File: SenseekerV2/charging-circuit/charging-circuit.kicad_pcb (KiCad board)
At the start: 2 copper layers, 40.8 x 83.5 mm, 91 parts, among them J1 2.54-1*6PHeader-RA, Q1 2N7002, Q2 CJQ4435, Q3 currentmirror, Q4 2N7002, Q5 CJQ4435, Q6 2N7002, Q7 CJQ4435, U1 MAX17048G+T10, U10 BQ25606RGER, U11 Battery Input, U2 MT3608, U3 MT3608, U6 MT3608, U7 2.54-2*20, U8 MAX3232CDBR, U9 ADS1115IDGSR

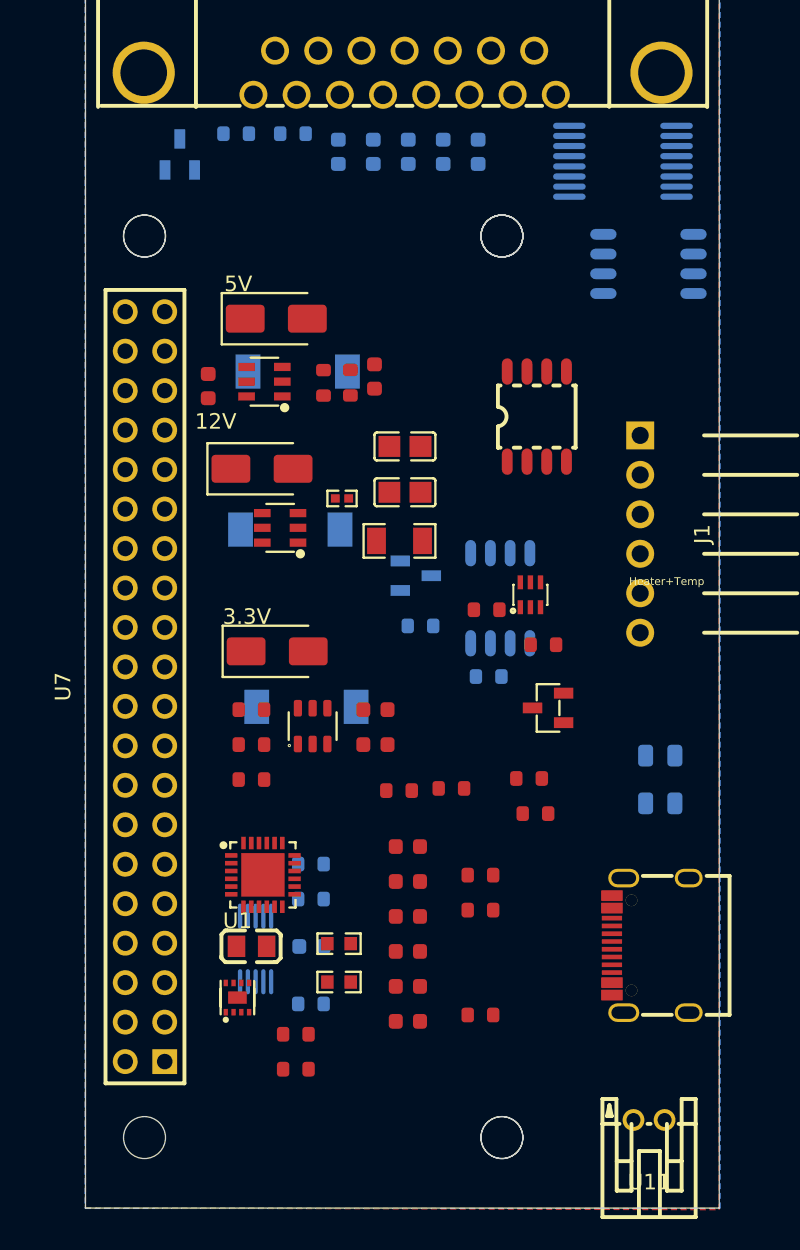
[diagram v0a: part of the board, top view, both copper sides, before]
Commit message: Initial Traces Complete
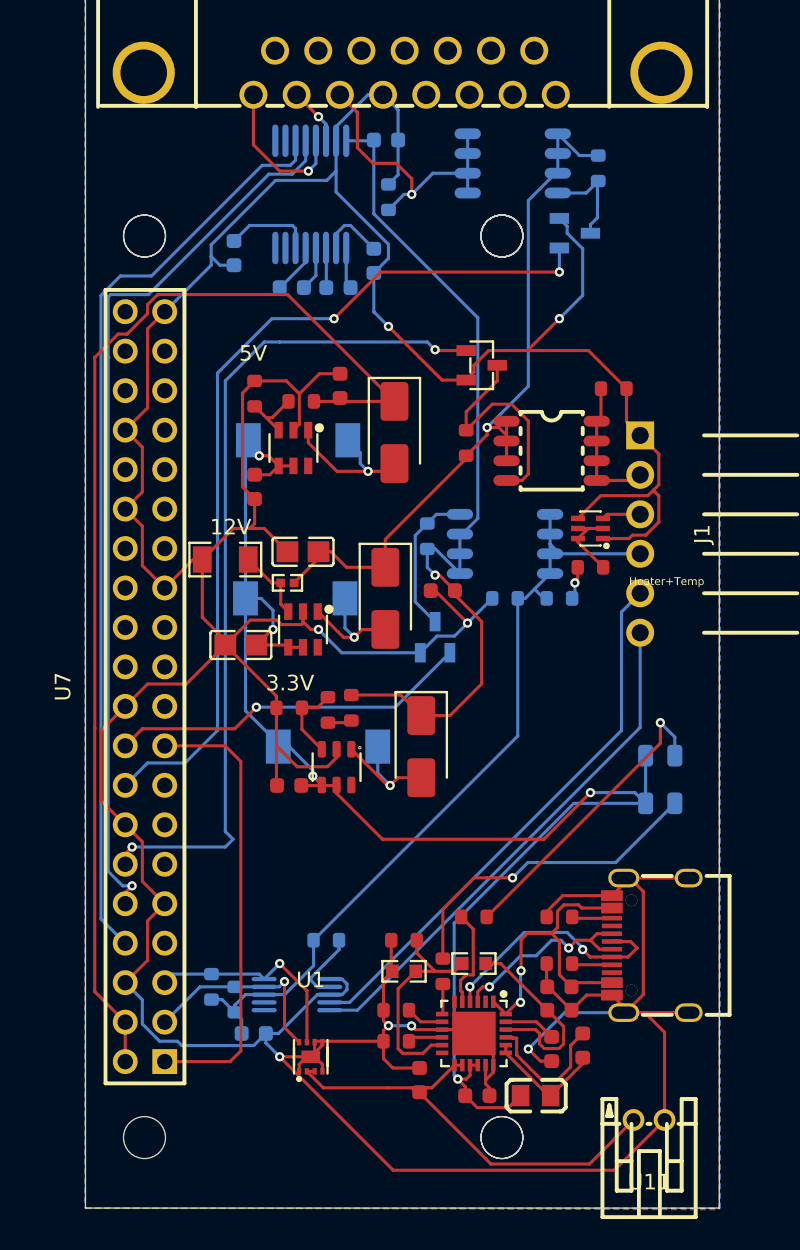
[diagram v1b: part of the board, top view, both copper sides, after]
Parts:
- R4: moved to B.Cu
- moved Q6 25.9 mm to (131.5, 90.5), turned to 180 degrees
- moved RPROG5 25.7 mm to (134.0, 100.5)
- moved R14 24.3 mm to (124.5, 104.0), turned to -90 degrees
- moved R15 23.4 mm to (133.0, 86.3), turned to 90 degrees
- moved Q1 22.5 mm to (125.5, 99.0), turned to 180 degrees
- moved L4 20.7 mm to (129.0, 146.0), turned to 180 degrees
- moved U8 20.2 mm to (114.5, 88.0), turned to 180 degrees
- moved R30 18.6 mm to (130.5, 134.5), turned to 180 degrees
- moved R31 18.3 mm to (130.5, 137.5), turned to 180 degrees
- moved U10 17.0 mm to (125.0, 142.0), turned to -90 degrees
- moved R22 16.7 mm to (120.0, 142.5)
- moved C2 16.6 mm to (110.0, 117.0), turned to 0 degrees
- moved C13 14.2 mm to (130.0, 143.0), turned to 90 degrees
- moved R25 14.1 mm to (120.0, 140.5)
- moved C9 13.3 mm to (130.5, 139.0)
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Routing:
- net GND: track 0.00 -> 353.5 mm, vias 0 -> 8
- net /VSYS: track 0.00 -> 99.9 mm, vias 0 -> 5
- net /5 Vout: track 0.00 -> 75.6 mm
- net /GPIO14/TXD0: track 0.00 -> 59.7 mm
- net /GPIO15/RXD0: track 0.00 -> 57.9 mm, vias 0 -> 1
- net /GPIO23: track 0.00 -> 56.6 mm, vias 0 -> 2
- net /3.3V: track 0.00 -> 55.9 mm, vias 0 -> 1
- net /GPIO18/PCM.CLK: track 0.00 -> 54.5 mm, vias 0 -> 2
- net /Temp3.3V: track 0.00 -> 52.7 mm
- net /12V: track 0.00 -> 47.1 mm, vias 0 -> 1
- net /A0: track 0.00 -> 35.4 mm
- net /A1: track 0.00 -> 33.6 mm
- net /raspi3.3V: track 0.00 -> 29.1 mm
- net /VBAT: track 0.00 -> 29.0 mm
- net /GPIO24: track 0.00 -> 23.4 mm, vias 0 -> 1
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
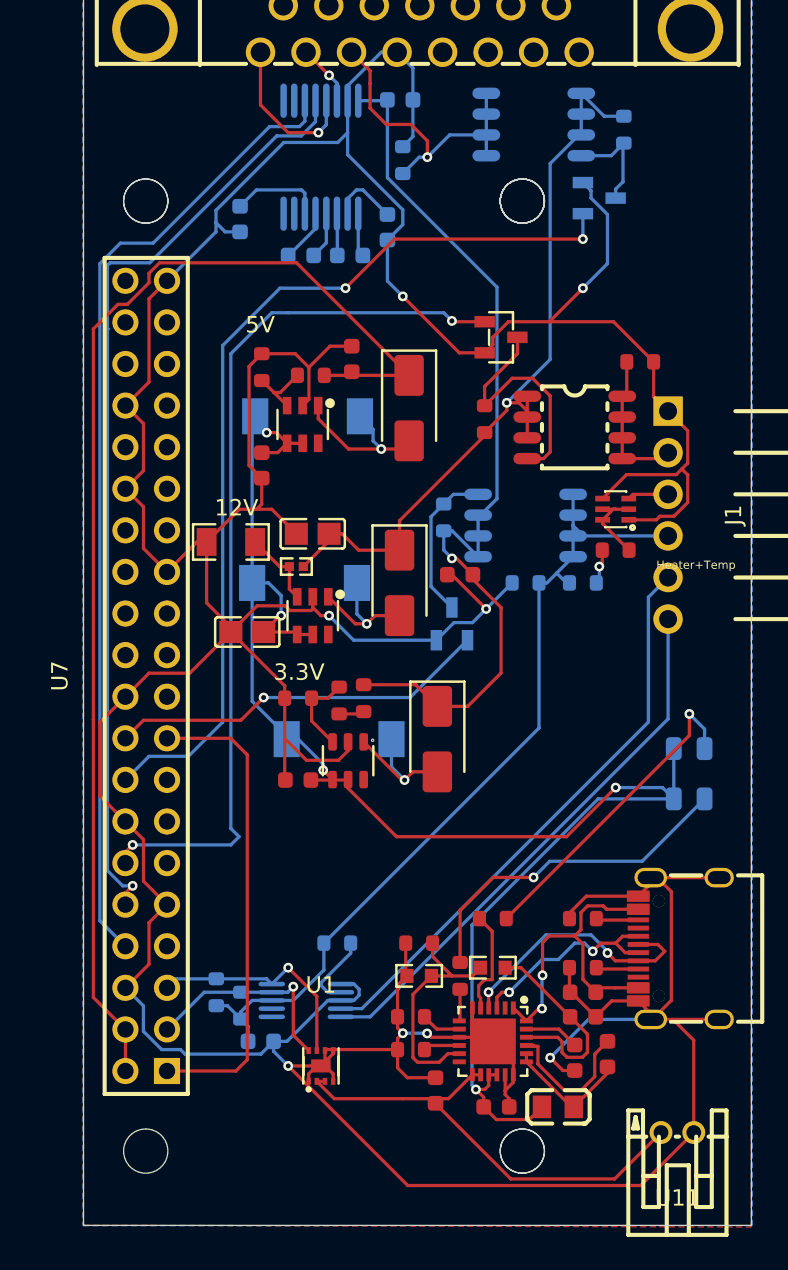
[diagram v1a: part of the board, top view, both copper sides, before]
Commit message: Fixed DRC Thermal Errors
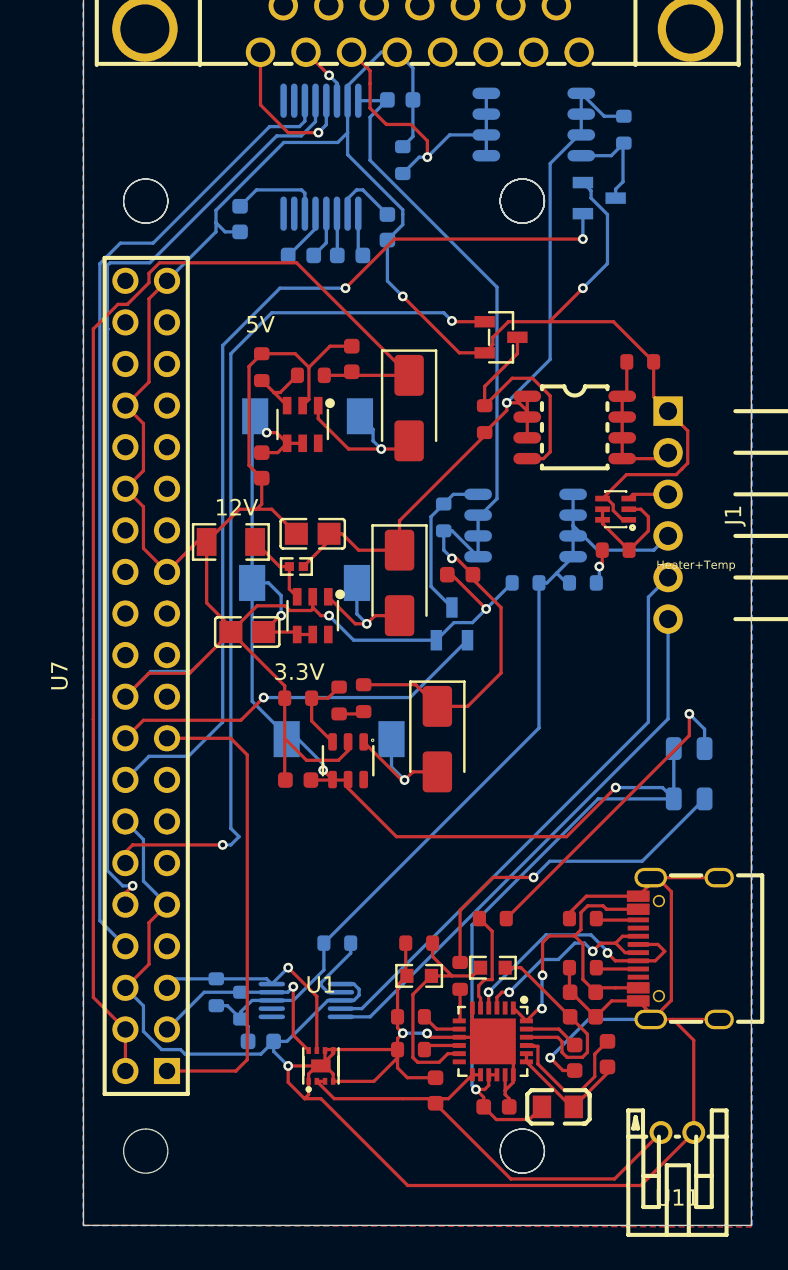
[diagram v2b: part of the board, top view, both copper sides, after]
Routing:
- net /base: track 5.19 -> 7.09 mm
- net GND: track 353.5 -> 352.2 mm
- net /3.3V: track 55.9 -> 56.7 mm
- net /Temp3.3V: track 52.7 -> 53.4 mm

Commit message: Final Edits to v2 before sending to Lucas
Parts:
- removed the ? at (40.1, 122.1)
- removed the ? at (63.1, 64.0) (x4)
- removed the ? at (40.1, 64.0) (x2)
- removed the ? at (63.1, 122.1) (x2)
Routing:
- net /VSYS: track 99.9 -> 100.6 mm
- net Net-(D8-Pad1): track 19.6 -> 20.3 mm

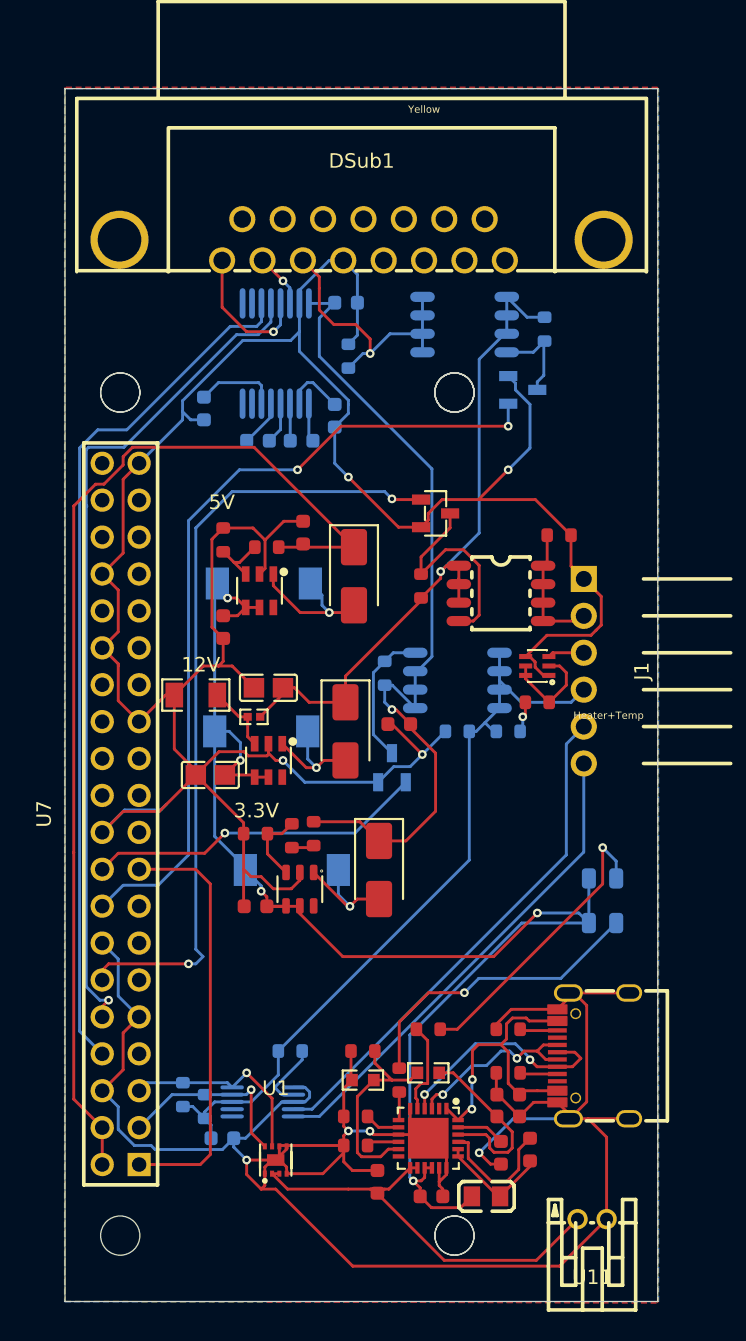
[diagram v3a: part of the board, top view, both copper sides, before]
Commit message: Brning in pcb from front of DSUB
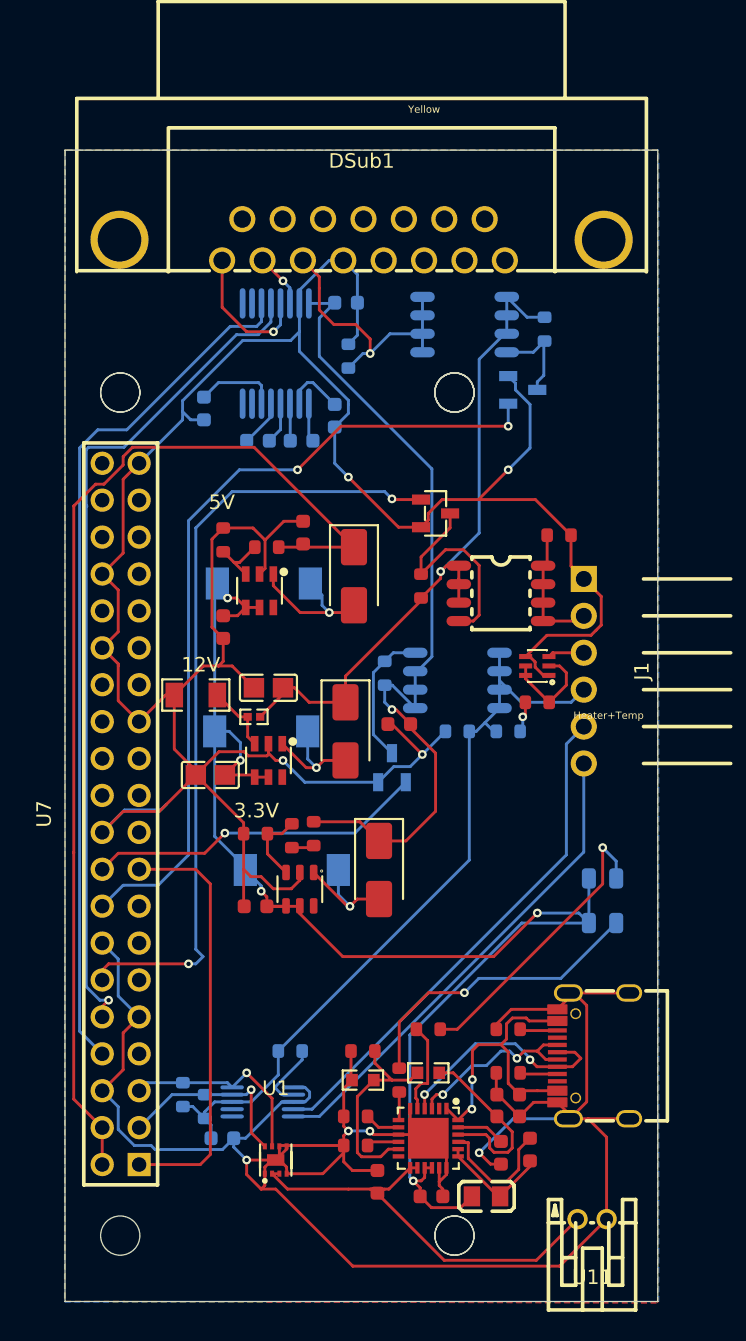
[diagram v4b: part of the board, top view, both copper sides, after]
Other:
- board size 40.8 x 83.5 mm -> 40.8 x 79.2 mm
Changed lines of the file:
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@@
 	)
 	(gr_rect
-		(start 100 69.76625)
+		(start 100 74)
 		(end 140.79 153.23625)
 		(stroke
@@
 		(polygon
 			(pts
-				(xy 100 69.668613) (xy 100 153.225476) (xy 140.78 153.342167) (xy 140.78 69.673819)
+				(xy 100 74) (xy 100 153.225476) (xy 140.78 153.342167) (xy 140.78 74)
 			)
 		)
@@
 		(polygon
 			(pts
-				(xy 99.97 69.768686) (xy 99.97 153.258686) (xy 140.85 153.258686) (xy 140.85 69.768686)
+				(xy 100 74) (xy 99.97 153.258686) (xy 140.85 153.258686) (xy 140.85 74)
 			)
 		)

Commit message: fixed dsub
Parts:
- removed DSub1: DS1037-15FNAKT74-0CC, easyeda2kicad:DSUB-TH_DS1037-15FNAKT74-0CC
- added DSub2: DS1038-15FBNSIA74-0CC, easyeda2kicad:DSUB-TH_DS1038-15FBNSIA74-0CC, F.Cu at (119.4, 77.7)
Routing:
- net /UART_RX_13V: track 9.61 -> 12.2 mm
- net Net-(DSub2-Pad3): track 19.1 -> 21.0 mm
- net /UART_TX_13V: track 3.74 -> 5.65 mm
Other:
- board size 40.8 x 79.2 mm -> 40.8 x 83.5 mm

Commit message: breakout
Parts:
- removed ? (x9): , 
- removed DSub2: DS1038-15FBNSIA74-0CC, easyeda2kicad:DSUB-TH_DS1038-15FBNSIA74-0CC
- removed Q4, Q6: 2N7002, easyeda2kicad:SOT-23-3_L2.9-W1.3-P1.90-LS2.4-BR
- removed Q5, Q7: CJQ4435, easyeda2kicad:SOP-8_L5.0-W4.0-P1.27-LS6.2-BL
- removed R15, R16: 10kΩ, PCM_JLCPCB:R_0603
- removed RPROG4, RPROG6: 1kΩ, PCM_JLCPCB:R_0603
- added C3: 100nF, PCM_JLCPCB:C_0603, F.Cu at (208.6, 127.5)
- added H1: Header-Male-2.54_1x6, easyeda2kicad:HDR-TH_6P-P2.54-V-M-1, F.Cu at (79.3, 73.7)
- added H2: 77311-462K05LF, easyeda2kicad:HDR-TH_5P-P2.54-V-M, F.Cu at (159.4, 126.0)
- added H3: Header-Male-2.54_1x6, easyeda2kicad:HDR-TH_6P-P2.54-V-M-1, F.Cu at (114.6, 35.2)
- added H4: Header-Male-2.54_1x6, easyeda2kicad:HDR-TH_6P-P2.54-V-M-1, F.Cu at (245.6, 76.1)
- added P1: Header-Male-2.54_2x2, easyeda2kicad:HDR-TH_4P-P2.54-V-M-R2-C2-S2.54-1, F.Cu at (67.2, 73.6)
- added P2: Header-Male-2.54_2x2, easyeda2kicad:HDR-TH_4P-P2.54-V-M-R2-C2-S2.54-1, F.Cu at (250.3, 112.0)
- added P3: 1.27mm/1*3p, easyeda2kicad:HDR-TH_3P-P1.27-V-M-1, F.Cu at (213.8, 118.0)
- added P5: 1.27mm/1*3p, easyeda2kicad:HDR-TH_3P-P1.27-V-M-1, F.Cu at (100.2, 41.3)
- added P6: 1.27mm/1*3p, easyeda2kicad:HDR-TH_3P-P1.27-V-M-1, F.Cu at (77.1, 41.3)
- added P7: 1.27mm/1*3p, easyeda2kicad:HDR-TH_3P-P1.27-V-M-1, F.Cu at (58.8, 36.5)
- added Q8: CJQ4435, easyeda2kicad:SOP-8_L5.0-W4.0-P1.27-LS6.2-BL, F.Cu at (219.5, 124.2)
- added R5: 44.2kohm, easyeda2kicad:R0402, F.Cu at (203.6, 125.8)
- added R6: 62kohm, easyeda2kicad:R0805, F.Cu at (204.4, 123.3)
- added R7: 30kΩ, PCM_JLCPCB:R_0603, F.Cu at (214.1, 121.1)
- added R8: 10kΩ, PCM_JLCPCB:R_0603, F.Cu at (214.1, 123.4)
- added R9: 10kΩ, PCM_JLCPCB:R_0603, F.Cu at (214.1, 125.6)
- added REF**: BreakLine_5h_D0.5mm_P0.85mm, MouseBites:BreakLine_5h_D0.5mm_P0.85mm, F.Cu at (64.0, 53.8)
- added REF**: BreakLine_5h_D0.5mm_P0.85mm, MouseBites:BreakLine_5h_D0.5mm_P0.85mm, F.Cu at (106.5, 53.8)
- added REF**: BreakLine_5h_D0.5mm_P0.85mm, MouseBites:BreakLine_5h_D0.5mm_P0.85mm, F.Cu at (104.3, 51.2)
- added REF**: BreakLine_5h_D0.5mm_P0.85mm, MouseBites:BreakLine_5h_D0.5mm_P0.85mm, F.Cu at (59.7, 53.8)
- added REF**: BreakLine_5h_D0.5mm_P0.85mm, MouseBites:BreakLine_5h_D0.5mm_P0.85mm, F.Cu at (55.5, 53.8)
- added REF**: BreakLine_5h_D0.5mm_P0.85mm, MouseBites:BreakLine_5h_D0.5mm_P0.85mm, F.Cu at (104.3, 33.9)
- added REF**: BreakLine_5h_D0.5mm_P0.85mm, MouseBites:BreakLine_5h_D0.5mm_P0.85mm, F.Cu at (97.8, 53.8)
- added REF**: BreakLine_5h_D0.5mm_P0.85mm, MouseBites:BreakLine_5h_D0.5mm_P0.85mm, F.Cu at (47.1, 53.8)
- added REF**: BreakLine_5h_D0.5mm_P0.85mm, MouseBites:BreakLine_5h_D0.5mm_P0.85mm, F.Cu at (104.3, 46.8)
- added REF**: BreakLine_5h_D0.5mm_P0.85mm, MouseBites:BreakLine_5h_D0.5mm_P0.85mm, F.Cu at (104.2, 42.3)
- added REF**: BreakLine_5h_D0.5mm_P0.85mm, MouseBites:BreakLine_5h_D0.5mm_P0.85mm, F.Cu at (93.5, 53.8)
- added REF**: BreakLine_5h_D0.5mm_P0.85mm, MouseBites:BreakLine_5h_D0.5mm_P0.85mm, F.Cu at (81.0, 53.8)
- added REF**: BreakLine_5h_D0.5mm_P0.85mm, MouseBites:BreakLine_5h_D0.5mm_P0.85mm, F.Cu at (110.8, 53.8)
- added REF**: BreakLine_5h_D0.5mm_P0.85mm, MouseBites:BreakLine_5h_D0.5mm_P0.85mm, F.Cu at (72.4, 53.8)
- added REF**: BreakLine_5h_D0.5mm_P0.85mm, MouseBites:BreakLine_5h_D0.5mm_P0.85mm, F.Cu at (115.0, 53.8)
- added REF**: BreakLine_5h_D0.5mm_P0.85mm, MouseBites:BreakLine_5h_D0.5mm_P0.85mm, F.Cu at (68.1, 53.8)
- added REF**: BreakLine_5h_D0.5mm_P0.85mm, MouseBites:BreakLine_5h_D0.5mm_P0.85mm, F.Cu at (85.1, 53.8)
- added REF**: BreakLine_5h_D0.5mm_P0.85mm, MouseBites:BreakLine_5h_D0.5mm_P0.85mm, F.Cu at (104.2, 37.9)
- added REF**: BreakLine_5h_D0.5mm_P0.85mm, MouseBites:BreakLine_5h_D0.5mm_P0.85mm, F.Cu at (123.4, 53.8)
- added REF**: BreakLine_5h_D0.5mm_P0.85mm, MouseBites:BreakLine_5h_D0.5mm_P0.85mm, F.Cu at (102.0, 53.8)
- added REF**: BreakLine_5h_D0.5mm_P0.85mm, MouseBites:BreakLine_5h_D0.5mm_P0.85mm, F.Cu at (119.3, 53.8)
- added REF**: BreakLine_5h_D0.5mm_P0.85mm, MouseBites:BreakLine_5h_D0.5mm_P0.85mm, F.Cu at (89.4, 53.8)
- added REF**: BreakLine_5h_D0.5mm_P0.85mm, MouseBites:BreakLine_5h_D0.5mm_P0.85mm, F.Cu at (51.3, 53.8)
- added REF**: BreakLine_5h_D0.5mm_P0.85mm, MouseBites:BreakLine_5h_D0.5mm_P0.85mm, F.Cu at (76.5, 53.8)
- added RPROG1: 1kΩ, PCM_JLCPCB:R_0603, F.Cu at (214.1, 127.9)
- added U4: TPL5110DDCT, easyeda2kicad:TSOT-23-6_L2.9-W1.6-P0.95-LS2.8-BR, F.Cu at (208.8, 123.9)
- added U5: BQ25606RGER, easyeda2kicad:VQFN-24_L4.0-W4.0-P0.50-TL-EP2.8, F.Cu at (104.9, 61.3)
- added mouse-bite-2mm-slot: VAL**, MouseBites:mouse-bite-2mm-slot, F.Cu at (26.7, 66.2)
- added mouse-bite-2mm-slot: VAL**, MouseBites:mouse-bite-2mm-slot, F.Cu at (28.4, 60.9)
- C12, C17, C18, C19, C20, C21, D8, D9, L1, L2, L3, R12, R13, R21, R4, U8, U9: moved to F.Cu
- U7: value 2.54-2*20 -> Z-21320110021001; footprint easyeda2kicad:HDR-TH_40P-P2.54-V-F-R2-C20-S2.54 -> easyeda2kicad:HDR-TH_20P-P2.54-V-M-R2-C10-S2.54
- moved R12 156.5 mm to (237.4, 50.8), turned to 0 degrees
- moved U9 154.1 mm to (242.4, 54.9), turned to 0 degrees
- moved C12 152.9 mm to (237.4, 56.1)
- moved R21 150.8 mm to (237.4, 59.8), turned to 0 degrees
- moved R13 147.4 mm to (237.4, 53.1)
- moved U1 134.1 mm to (245.1, 112.8)
- moved Q2 129.2 mm to (247.5, 50.7), turned to 0 degrees
- moved J1 129.2 mm to (254.1, 58.3)
- moved R14 127.0 mm to (248.8, 77.7), turned to 0 degrees
- moved Q1 126.2 mm to (248.2, 69.5), turned to 0 degrees
- moved R4 125.3 mm to (245.7, 64.6)
- moved R23 125.2 mm to (249.3, 66.8)
- moved Q3 124.0 mm to (247.1, 62.2), turned to 0 degrees
- moved RPROG5 117.1 mm to (248.4, 75.4)
- moved D6 113.1 mm to (49.8, 36.1), turned to 0 degrees
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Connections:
- C1 pad 1: GND -> /12GND
- C1 pad 2: /12V -> /12VOUT
- C10 pad 1: /VSYS -> /3V3VSYS
- C10 pad 2: GND -> /3V3GND
- C11 pad 1: GND -> /3V3GND
- C11 pad 2: /3.3V -> /3V3VOUT
- C12 pad 2: GND -> /Address
- C13 pad 1: GND -> /GND1
- C14 pad 1: GND -> /GND1
- C14 pad 2: /VBAT -> /VBAT1
- C15 pad 2: GND -> /GND1
- C17 pad 2: GND -> /DSUBGND
- C18 pad 2: GND -> /DSUBGND
- C2 pad 1: GND -> /12GND
- C2 pad 2: /VSYS -> /12VSYS
- C21 pad 2: GND -> /DSUBGND
- C22 pad 1: GND -> /GND1
- C22 pad 2: /VSYS -> /VSYS1
- C4 pad 1: GND -> /5GND
- C4 pad 2: /5 Vout -> /5VOUT
- C7 pad 1: /VSYS -> /5VSYS
- C7 pad 2: GND -> /5GND
- C9 pad 1: GND -> /GND1
- C9 pad 2: /VBUS -> /VBUS1
- D4 pad 1: /12V -> /12VOUT
- D5 pad 1: /5 Vout -> /5VOUT
- D6 pad 1: /3.3V -> /3V3VOUT
- D8 pad 2: /VSYS -> /VSYS1
- D9 pad 2: /VSYS -> /VSYS1
- J1 pad 1: GND -> /Address
- L1 pad 1: /VSYS -> /5VSYS
- L2 pad 1: /VSYS -> /12VSYS
- L3 pad 1: /VSYS -> /3V3VSYS
- L4 pad 2: /VSYS -> /VSYS1
- Q1 pad 1: /GPIO18/PCM.CLK -> /PWMSIG
- Q1 pad 2: GND -> /Address
- Q2 pad 1: /12V -> /TEMP12V
- Q2 pad 2: /12V -> /TEMP12V
- Q2 pad 3: /12V -> /TEMP12V
- Q3 pad 1: GND -> /Address
- Q3 pad 4: GND -> /Address
- R1 pad 1: GND -> /12GND
- R10 pad 1: /5 Vout -> /5VOUT
- R12 pad 2: /GPIO3/SCL1 -> /TEMPSCL
- R14 pad 2: /12V -> /TEMP12V
- R18 pad 1: /3.3V -> /3V3VOUT
- R19 pad 2: GND -> /3V3GND
- R2 pad 1: /12V -> /12VOUT
- R21 pad 2: /GPIO2/SDA1 -> /TEMPSDA
- R22 pad 1: GND -> /GND1
- R25 pad 1: GND -> /GND1
- R27 pad 1: /REGN -> /REGN1
- R28 pad 2: GND -> /GND1
- R29 pad 2: GND -> /GND1
- R3 pad 2: GND -> /5GND
- R30 pad 2: GND -> /USBGND
- R31 pad 2: GND -> /USBGND
- RPROG5 pad 2: GND -> /Address
- U1 pad 1: GND -> /FUELGND
- U1 pad 2: /VBAT -> /FUELBAT
- U1 pad 3: /VBAT -> /FUELBAT
- U1 pad 4: GND -> /FUELGND
- U1 pad 5: GND -> /FUELGND
- U1 pad 6: GND -> /FUELGND
- U1 pad 7: /GPIO3/SCL1 -> /FUELSCL
- U1 pad 8: /GPIO2/SDA1 -> /FUELSDA
- U1 pad 9: GND -> /FUELGND
- U10 pad 1: /VBUS -> /VBUS1
- U10 pad 13: /VBAT -> /VBAT1
- U10 pad 14: /VBAT -> /VBAT1
- U10 pad 15: /VSYS -> /VSYS1
- U10 pad 16: /VSYS -> /VSYS1
- U10 pad 17: GND -> /GND1
- U10 pad 18: GND -> /GND1
- U10 pad 24: /VBUS -> /VBUS1
- U10 pad 25: GND -> /GND1
- U10 pad 3: /D+ -> /1D+
- U10 pad 4: /D- -> /1D-
- U10 pad 6: GND -> unconnected-(U10-OTG-Pad6)
- U10 pad 9: GND -> /GND1
- U11 pad 2: GND -> /USBGND
- U2 pad 2: GND -> /5GND
- U2 pad 4: /VSYS -> /5VSYS
- U2 pad 5: /VSYS -> /5VSYS
- U3 pad 2: GND -> /12GND
- U3 pad 4: /VSYS -> /12VSYS
- U3 pad 5: /VSYS -> /12VSYS
- U6 pad 2: GND -> /3V3GND
- U6 pad 4: /VSYS -> /3V3VSYS
- U6 pad 5: /VSYS -> /3V3VSYS
- U7 pad 1: /raspi3.3V -> /VAC2
- U7 pad 10: /GPIO15/RXD0 -> /ICHG2
- U7 pad 11: /GPIO17 -> /TS2
- U7 pad 12: /GPIO18/PCM.CLK -> /VSET2
- U7 pad 13: /GPIO27 -> /BAT2
- U7 pad 14: GND -> /SYS2
- U7 pad 15: /GPIO22 -> /GND2
- U7 pad 16: /GPIO23 -> /SW2
- U7 pad 17: /raspi3.3V -> /BTST
- U7 pad 18: /GPIO24 -> /REGN2
- U7 pad 19: /GPIO10/SPI0.MOSI -> /PMID2
- U7 pad 2: /5 Vout -> /NC2
- U7 pad 20: GND -> /VBUS2
- U7 pad 3: /GPIO2/SDA1 -> /2D+
- U7 pad 4: /5 Vout -> /2D-
- U7 pad 5: /GPIO3/SCL1 -> /STAT2
- U7 pad 6: GND -> /OTG2
- U7 pad 7: /GPIO4/GPCLK0 -> /PG2
- U7 pad 8: /GPIO14/TXD0 -> /ILIM2
- U7 pad 9: GND -> /CE2
- U8 pad 11: /GPIO14/TXD0 -> /TX
- U8 pad 12: /GPIO15/RXD0 -> /RX
- U8 pad 15: GND -> /DSUBGND
- U9 pad 1: GND -> /Address
- U9 pad 10: /GPIO3/SCL1 -> /TEMPSCL
- U9 pad 9: /GPIO2/SDA1 -> /TEMPSDA
- USBC1 pad 1: GND -> /USBGND
- USBC1 pad 2: GND -> /USBGND
- USBC1 pad 3: GND -> /USBGND
- USBC1 pad 4: GND -> /USBGND
- USBC1 pad A1B12: GND -> /USBGND
- USBC1 pad B1A12: GND -> /USBGND
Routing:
- net GND: track 352.2 -> 0.00 mm, vias 8 -> 0
- net /VSYS: track 100.6 -> 0.00 mm, vias 5 -> 0
- net /5 Vout: track 75.6 -> 0.00 mm
- net /GPIO14/TXD0: track 59.7 -> 0.00 mm
- net /GPIO15/RXD0: track 57.9 -> 0.00 mm, vias 1 -> 0
- net /3.3V: track 56.7 -> 0.00 mm, vias 1 -> 0
- net /GPIO23: track 56.6 -> 0.00 mm, vias 2 -> 0
- net /GPIO18/PCM.CLK: track 54.5 -> 0.00 mm, vias 2 -> 0
- net /Temp3.3V: track 53.4 -> 0.00 mm
- net /12V: track 47.1 -> 0.00 mm, vias 1 -> 0
- net /A0: track 35.4 -> 0.00 mm
- net /A1: track 33.6 -> 0.00 mm
- net /raspi3.3V: track 29.1 -> 0.00 mm
- net /VBAT: track 29.0 -> 0.00 mm
- net /GPIO24: track 23.4 -> 0.00 mm, vias 1 -> 0
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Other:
- board size 40.8 x 83.5 mm -> 80.8 x 45.9 mm
- board text added: "SenseekerTest"
- board text removed: "12V"
- board text removed: "3.3V"
- board text removed: "5V"
- board text removed: "Green"
- board text removed: "Heater+Temp"
- board text removed: "PG"
- board text removed: "Red"
- board text removed: "STAT"
- board text removed: "Senseeker V2"
